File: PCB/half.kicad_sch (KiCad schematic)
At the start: 95 parts, among them J3 JST_PH, SW1 SW_Push, SW10 SW_Push, SW11 SW_Push, SW12 SW_Push, SW13 SW_Push, SW14 SW_Push, SW15 SW_Push, SW16 SW_Push, SW17 SW_Push, SW18 SW_Push, SW19 SW_Push, SW2 SW_Push, SW20 SW_Push, SW21 SW_Push, SW22 SW_Push, SW23 SW_Push, SW24 SW_Push, SW25 SW_Push, SW26 SW_Push, SW27 SW_Push, SW28 SW_Push, SW29 SW_Push, SW3 SW_Push, SW4 SW_Push, SW5 SW_Push, SW59 RotaryEncoder_Switch, SW6 SW_Push, SW61 SW_SPDT, SW7 SW_Push, SW8 SW_Push, SW9 SW_Push, U3 SuperMini nRF52840

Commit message: switch identifier positioned
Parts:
- renumbered SW6 to SW1, SW18 to SW13, SW13 to SW14, SW24 to SW16, SW1 to SW2, SW19 to SW20, SW25 to SW26, SW2 to SW3, SW12 to SW7, SW7 to SW8
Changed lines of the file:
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@@
 		(dnp no)
 		(fields_autoplaced yes)
-		(property "Reference" "SW18"
+		(property "Reference" "SW13"
 			(at 144.78 125.73 0)
 			(effects
@@
 				)
 				(path "/fade6638-4e22-4fdd-8807-944beeb130ad/7560e8d7-2115-4052-abf3-3690798ba6d5"
-					(reference "SW18")
+					(reference "SW13")
 					(unit 1)
 				)
@@
 		(dnp no)
 		(fields_autoplaced yes)
-		(property "Reference" "SW24"
+		(property "Reference" "SW16"
 			(at 144.78 144.78 0)
 			(effects
@@
 				)
 				(path "/fade6638-4e22-4fdd-8807-944beeb130ad/7560e8d7-2115-4052-abf3-3690798ba6d5"
-					(reference "SW24")
+					(reference "SW16")
 					(unit 1)
 				)
@@
 		(dnp no)
 		(fields_autoplaced yes)
-		(property "Reference" "SW25"
+		(property "Reference" "SW26"
 			(at 36.83 163.83 0)
 			(effects
@@
 				)
 				(path "/fade6638-4e22-4fdd-8807-944beeb130ad/7560e8d7-2115-4052-abf3-3690798ba6d5"
-					(reference "SW25")
+					(reference "SW26")
 					(unit 1)
 				)
@@
 		(dnp no)
 		(fields_autoplaced yes)
-		(property "Reference" "SW12"
+		(property "Reference" "SW7"
 			(at 144.78 106.68 0)
 			(effects
@@
 				)
 				(path "/fade6638-4e22-4fdd-8807-944beeb130ad/7560e8d7-2115-4052-abf3-3690798ba6d5"
-					(reference "SW12")
+					(reference "SW7")
 					(unit 1)
 				)
@@
 		(dnp no)
 		(fields_autoplaced yes)
-		(property "Reference" "SW13"
+		(property "Reference" "SW14"
 			(at 36.83 125.73 0)
 			(effects
@@
 				)
 				(path "/fade6638-4e22-4fdd-8807-944beeb130ad/7560e8d7-2115-4052-abf3-3690798ba6d5"
-					(reference "SW13")
+					(reference "SW14")
 					(unit 1)
 				)
@@
 		(dnp no)
 		(fields_autoplaced yes)
-		(property "Reference" "SW19"
+		(property "Reference" "SW20"
 			(at 36.83 144.78 0)
 			(effects
@@
 				)
 				(path "/fade6638-4e22-4fdd-8807-944beeb130ad/7560e8d7-2115-4052-abf3-3690798ba6d5"
-					(reference "SW19")
+					(reference "SW20")
 					(unit 1)
 				)
@@
 		(dnp no)
 		(fields_autoplaced yes)
-		(property "Reference" "SW6"
+		(property "Reference" "SW1"
 			(at 144.78 87.63 0)
 			(effects
@@
 				)
 				(path "/fade6638-4e22-4fdd-8807-944beeb130ad/7560e8d7-2115-4052-abf3-3690798ba6d5"
-					(reference "SW6")
+					(reference "SW1")
 					(unit 1)
 				)
@@
 		(dnp no)
 		(fields_autoplaced yes)
-		(property "Reference" "SW1"
+		(property "Reference" "SW2"
 			(at 36.83 87.63 0)
 			(effects
@@
 				)
 				(path "/fade6638-4e22-4fdd-8807-944beeb130ad/7560e8d7-2115-4052-abf3-3690798ba6d5"
-					(reference "SW1")
+					(reference "SW2")
 					(unit 1)
 				)
@@
 		(dnp no)
 		(fields_autoplaced yes)
-		(property "Reference" "SW7"
+		(property "Reference" "SW8"
 			(at 36.83 106.68 0)
 			(effects
@@
 				)
 				(path "/fade6638-4e22-4fdd-8807-944beeb130ad/7560e8d7-2115-4052-abf3-3690798ba6d5"
-					(reference "SW7")
+					(reference "SW8")
 					(unit 1)
 				)
@@
 		(dnp no)
 		(fields_autoplaced yes)
-		(property "Reference" "SW2"
+		(property "Reference" "SW3"
 			(at 58.42 87.63 0)
 			(effects
@@
 				)
 				(path "/fade6638-4e22-4fdd-8807-944beeb130ad/7560e8d7-2115-4052-abf3-3690798ba6d5"
-					(reference "SW2")
+					(reference "SW3")
 					(unit 1)
 				)

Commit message: switch aligned with led
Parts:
- renumbered SW9 to SW10, SW10 to SW11, SW11 to SW12, SW14 to SW15, SW15 to SW16, SW16 to SW17, SW17 to SW18, SW16 to SW19, SW20 to SW21, SW21 to SW22, SW22 to SW23, SW23 to SW24, SW26 to SW25, SW3 to SW4, SW4 to SW5, SW5 to SW6, SW8 to SW9
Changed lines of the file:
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@@
 		(dnp no)
 		(fields_autoplaced yes)
-		(property "Reference" "SW11"
+		(property "Reference" "SW12"
 			(at 123.19 106.68 0)
 			(effects
@@
 				)
 				(path "/fade6638-4e22-4fdd-8807-944beeb130ad/7560e8d7-2115-4052-abf3-3690798ba6d5"
-					(reference "SW11")
+					(reference "SW12")
 					(unit 1)
 				)
@@
 		(dnp no)
 		(fields_autoplaced yes)
-		(property "Reference" "SW3"
+		(property "Reference" "SW4"
 			(at 80.01 87.63 0)
 			(effects
@@
 				)
 				(path "/fade6638-4e22-4fdd-8807-944beeb130ad/7560e8d7-2115-4052-abf3-3690798ba6d5"
-					(reference "SW3")
+					(reference "SW4")
 					(unit 1)
 				)
@@
 		(dnp no)
 		(fields_autoplaced yes)
-		(property "Reference" "SW15"
+		(property "Reference" "SW16"
 			(at 80.01 125.73 0)
 			(effects
@@
 				)
 				(path "/fade6638-4e22-4fdd-8807-944beeb130ad/7560e8d7-2115-4052-abf3-3690798ba6d5"
-					(reference "SW15")
+					(reference "SW16")
 					(unit 1)
 				)
@@
 		(dnp no)
 		(fields_autoplaced yes)
-		(property "Reference" "SW20"
+		(property "Reference" "SW21"
 			(at 58.42 144.78 0)
 			(effects
@@
 				)
 				(path "/fade6638-4e22-4fdd-8807-944beeb130ad/7560e8d7-2115-4052-abf3-3690798ba6d5"
-					(reference "SW20")
+					(reference "SW21")
 					(unit 1)
 				)
@@
 		(dnp no)
 		(fields_autoplaced yes)
-		(property "Reference" "SW4"
+		(property "Reference" "SW5"
 			(at 101.6 87.63 0)
 			(effects
@@
 				)
 				(path "/fade6638-4e22-4fdd-8807-944beeb130ad/7560e8d7-2115-4052-abf3-3690798ba6d5"
-					(reference "SW4")
+					(reference "SW5")
 					(unit 1)
 				)
@@
 		(dnp no)
 		(fields_autoplaced yes)
-		(property "Reference" "SW16"
+		(property "Reference" "SW17"
 			(at 101.6 125.73 0)
 			(effects
@@
 				)
 				(path "/fade6638-4e22-4fdd-8807-944beeb130ad/7560e8d7-2115-4052-abf3-3690798ba6d5"
-					(reference "SW16")
+					(reference "SW17")
 					(unit 1)
 				)
@@
 		(dnp no)
 		(fields_autoplaced yes)
-		(property "Reference" "SW9"
+		(property "Reference" "SW10"
 			(at 80.01 106.68 0)
 			(effects
@@
 				)
 				(path "/fade6638-4e22-4fdd-8807-944beeb130ad/7560e8d7-2115-4052-abf3-3690798ba6d5"
-					(reference "SW9")
+					(reference "SW10")
 					(unit 1)
 				)
@@
 		(dnp no)
 		(fields_autoplaced yes)
-		(property "Reference" "SW16"
+		(property "Reference" "SW19"
 			(at 144.78 144.78 0)
 			(effects
@@
 				)
 				(path "/fade6638-4e22-4fdd-8807-944beeb130ad/7560e8d7-2115-4052-abf3-3690798ba6d5"
-					(reference "SW16")
+					(reference "SW19")
 					(unit 1)
 				)
@@
 		(dnp no)
 		(fields_autoplaced yes)
-		(property "Reference" "SW26"
+		(property "Reference" "SW25"
 			(at 36.83 163.83 0)
 			(effects
@@
 				)
 				(path "/fade6638-4e22-4fdd-8807-944beeb130ad/7560e8d7-2115-4052-abf3-3690798ba6d5"
-					(reference "SW26")
+					(reference "SW25")
 					(unit 1)
 				)
@@
 		(dnp no)
 		(fields_autoplaced yes)
-		(property "Reference" "SW14"
+		(property "Reference" "SW15"
 			(at 58.42 125.73 0)
 			(effects
@@
 				)
 				(path "/fade6638-4e22-4fdd-8807-944beeb130ad/7560e8d7-2115-4052-abf3-3690798ba6d5"
-					(reference "SW14")
+					(reference "SW15")
 					(unit 1)
 				)
@@
 		(dnp no)
 		(fields_autoplaced yes)
-		(property "Reference" "SW22"
+		(property "Reference" "SW23"
 			(at 101.6 144.78 0)
 			(effects
@@
 				)
 				(path "/fade6638-4e22-4fdd-8807-944beeb130ad/7560e8d7-2115-4052-abf3-3690798ba6d5"
-					(reference "SW22")
+					(reference "SW23")
 					(unit 1)
 				)
@@
 		(dnp no)
 		(fields_autoplaced yes)
-		(property "Reference" "SW23"
+		(property "Reference" "SW24"
 			(at 123.19 144.78 0)
 			(effects
@@
 				)
 				(path "/fade6638-4e22-4fdd-8807-944beeb130ad/7560e8d7-2115-4052-abf3-3690798ba6d5"
-					(reference "SW23")
+					(reference "SW24")
 					(unit 1)
 				)
@@
 		(dnp no)
 		(fields_autoplaced yes)
-		(property "Reference" "SW8"
+		(property "Reference" "SW9"
 			(at 58.42 106.68 0)
 			(effects
@@
 				)
 				(path "/fade6638-4e22-4fdd-8807-944beeb130ad/7560e8d7-2115-4052-abf3-3690798ba6d5"
-					(reference "SW8")
+					(reference "SW9")
 					(unit 1)
 				)
@@
 		(dnp no)
 		(fields_autoplaced yes)
-		(property "Reference" "SW5"
+		(property "Reference" "SW6"
 			(at 123.19 87.63 0)
 			(effects
@@
 				)
 				(path "/fade6638-4e22-4fdd-8807-944beeb130ad/7560e8d7-2115-4052-abf3-3690798ba6d5"
-					(reference "SW5")
+					(reference "SW6")
 					(unit 1)
 				)
@@
 		(dnp no)
 		(fields_autoplaced yes)
-		(property "Reference" "SW10"
+		(property "Reference" "SW11"
 			(at 101.6 106.68 0)
 			(effects
@@
 				)
 				(path "/fade6638-4e22-4fdd-8807-944beeb130ad/7560e8d7-2115-4052-abf3-3690798ba6d5"
-					(reference "SW10")
+					(reference "SW11")
 					(unit 1)
 				)
@@
 		(dnp no)
 		(fields_autoplaced yes)
-		(property "Reference" "SW17"
+		(property "Reference" "SW18"
 			(at 123.19 125.73 0)
 			(effects
@@
 				)
 				(path "/fade6638-4e22-4fdd-8807-944beeb130ad/7560e8d7-2115-4052-abf3-3690798ba6d5"
-					(reference "SW17")
+					(reference "SW18")
 					(unit 1)
 				)
@@
 		(dnp no)
 		(fields_autoplaced yes)
-		(property "Reference" "SW21"
+		(property "Reference" "SW22"
 			(at 80.01 144.78 0)
 			(effects
@@
 				)
 				(path "/fade6638-4e22-4fdd-8807-944beeb130ad/7560e8d7-2115-4052-abf3-3690798ba6d5"
-					(reference "SW21")
+					(reference "SW22")
 					(unit 1)
 				)

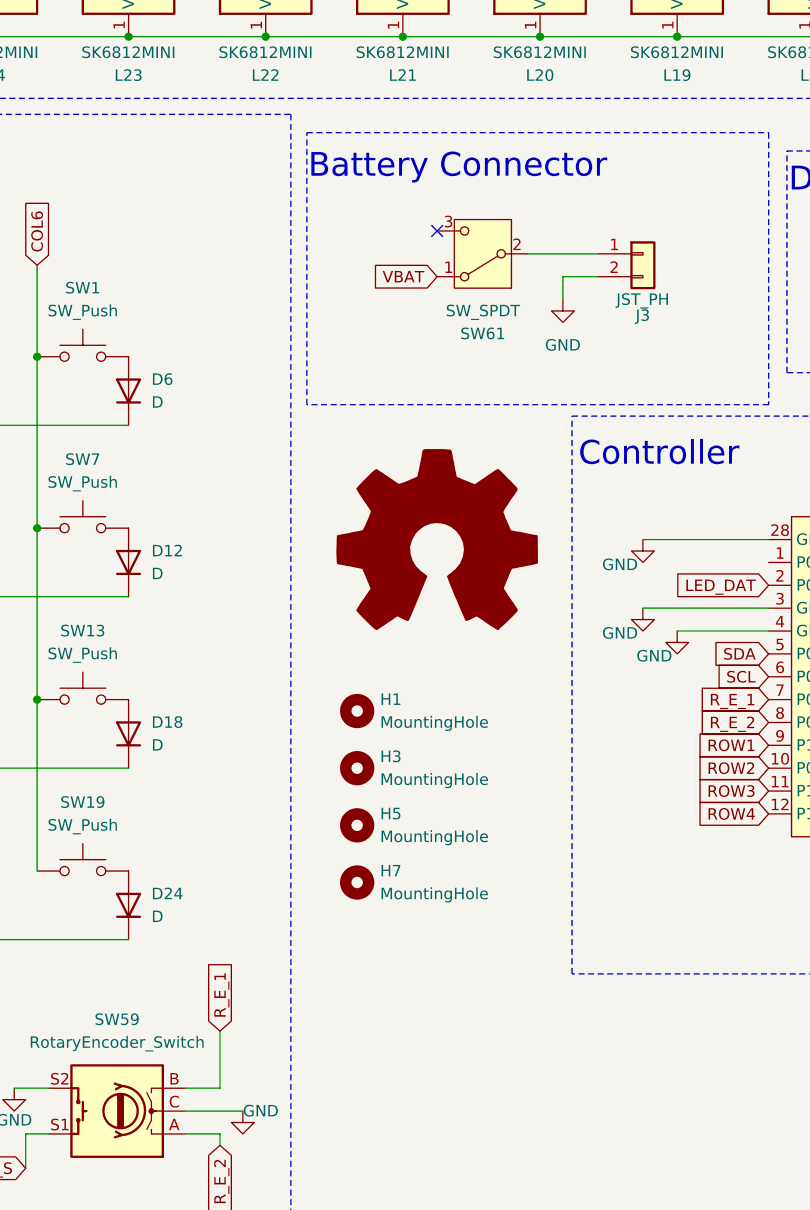
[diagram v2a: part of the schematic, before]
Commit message: prepare complete redesign
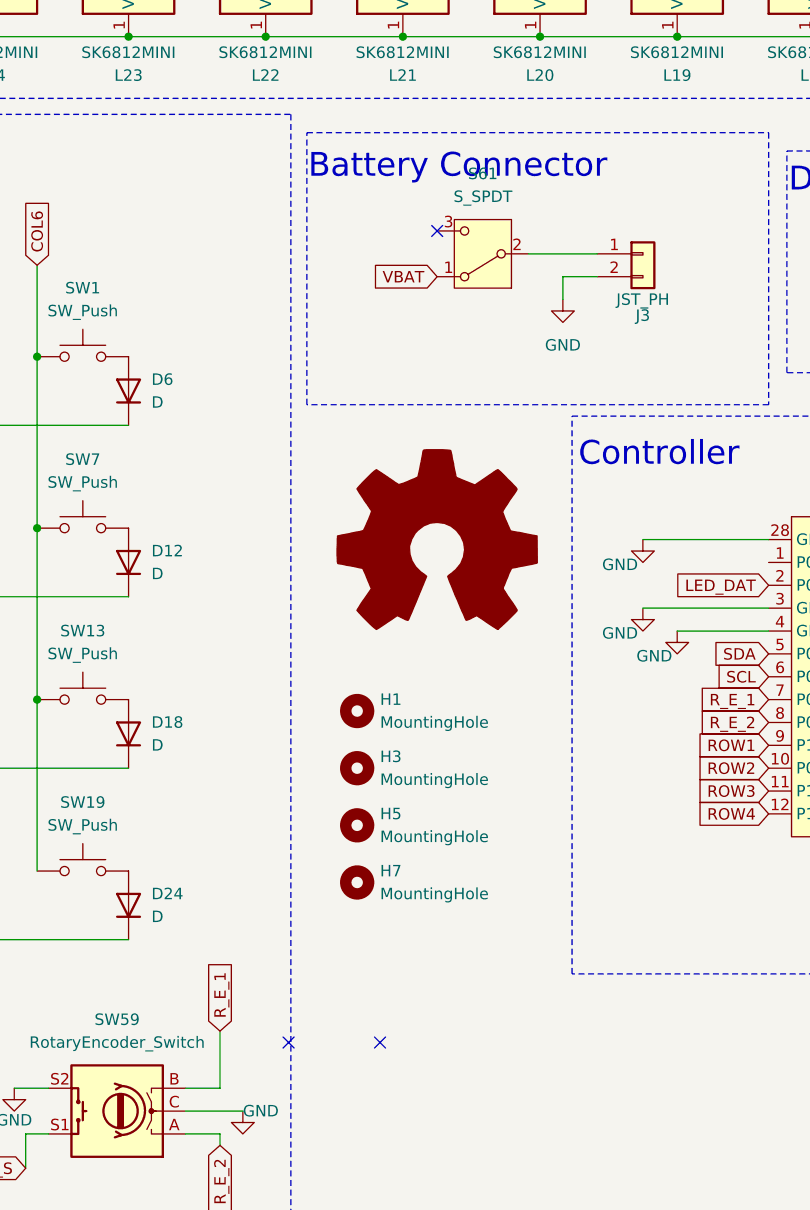
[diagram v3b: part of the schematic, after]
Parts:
- S61: renamed from SW61; value SW_SPDT -> S_SPDT
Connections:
- no-connect marks 3 -> 5
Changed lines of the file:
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@@
+	)
+	(no_connect
+		(at 167.64 171.45)
 	)
 	(no_connect
 		(at 184.15 81.28)
+	)
+	(no_connect
+		(at 177.8 171.45)
 	)
 	(wire
@@
 		(dnp no)
 		(fields_autoplaced yes)
-		(property "Reference" "SW61"
-			(at 189.23 92.71 0)
-			(effects
-				(font
-					(size 1.27 1.27)
-				)
-			)
-		)
-		(property "Value" "SW_SPDT"
-			(at 189.23 90.17 0)
+		(property "Reference" "S61"
+			(at 189.23 74.93 0)
+			(effects
+				(font
+					(size 1.27 1.27)
+				)
+			)
+		)
+		(property "Value" "S_SPDT"
+			(at 189.23 77.47 0)
 			(effects
 				(font
@@
 			(project ""
 				(path "/fade6638-4e22-4fdd-8807-944beeb130ad/0032fa72-ac59-4218-be72-f997fa7d8d03"
-					(reference "SW62")
+					(reference "S62")
 					(unit 1)
 				)
 				(path "/fade6638-4e22-4fdd-8807-944beeb130ad/7560e8d7-2115-4052-abf3-3690798ba6d5"
-					(reference "SW61")
+					(reference "S61")
 					(unit 1)
 				)
